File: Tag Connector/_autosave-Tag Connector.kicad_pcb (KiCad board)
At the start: 2 copper layers, 44.5 x 25.1 mm, 3 parts, among them J1 Conn_01x05_Male, J2 Conn_01x05_Male

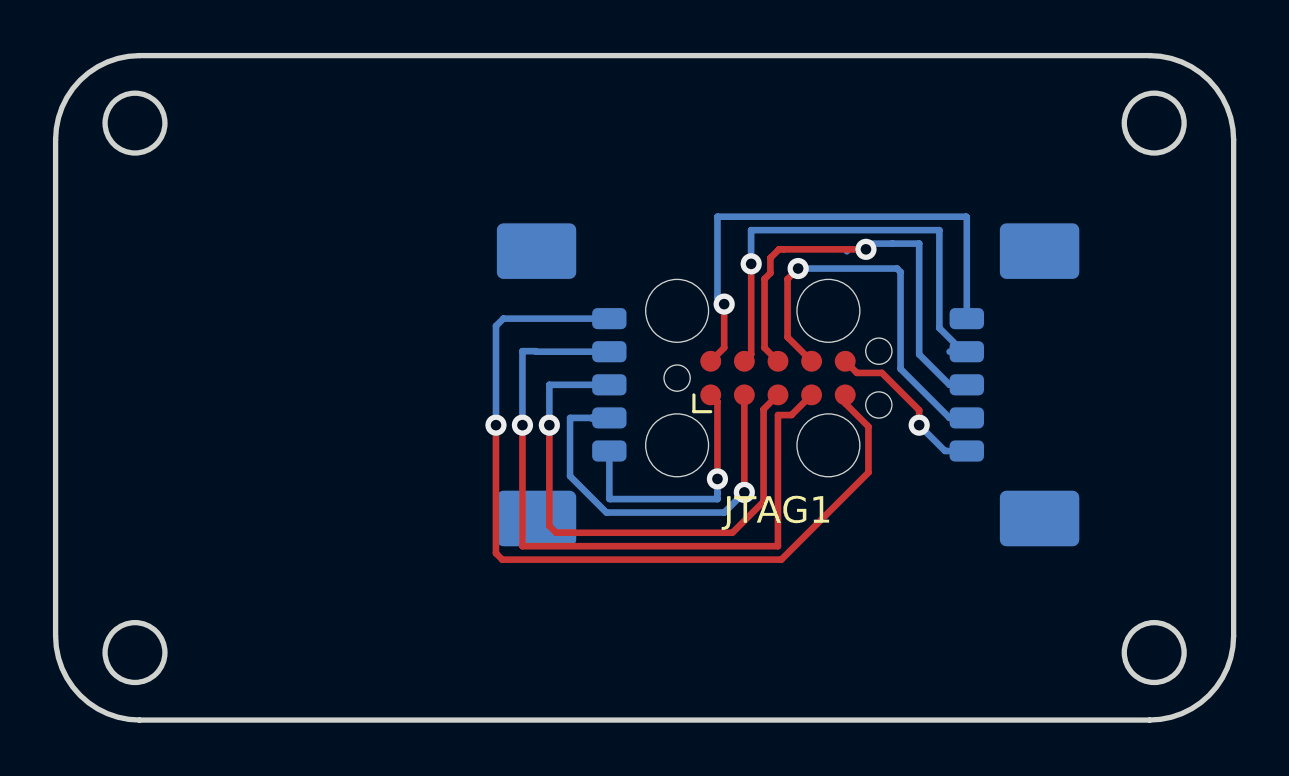
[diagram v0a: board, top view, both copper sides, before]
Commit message: updated manufacturing files
used correct dxf file to adjust the mounting holes on the PCB
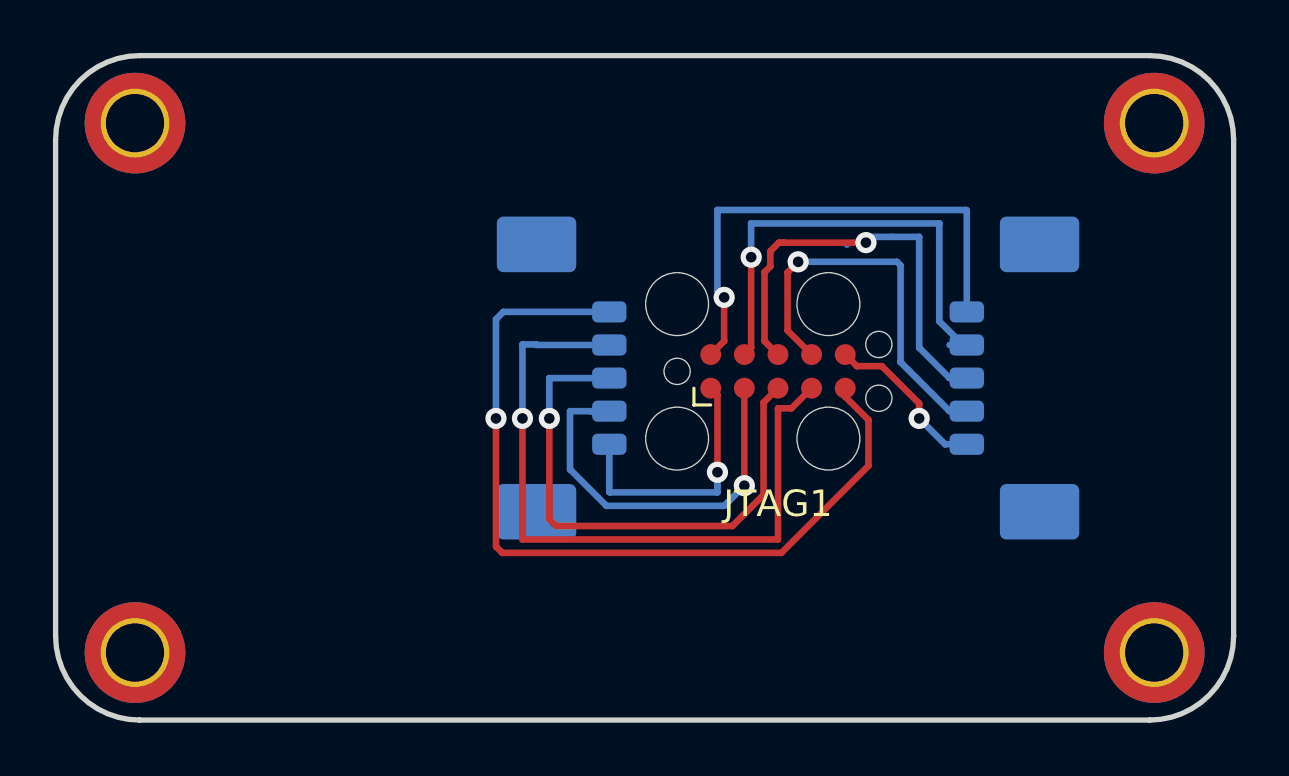
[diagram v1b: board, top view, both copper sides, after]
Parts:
- added ?: MountingHole_2.2mm_M2_DIN965_Pad_TopBottom, MountingHole:MountingHole_2.2mm_M2_DIN965_Pad_TopBottom, F.Cu at (136.9, 57.6)
- added REF**: MountingHole_2.2mm_M2_DIN965_Pad_TopBottom, MountingHole:MountingHole_2.2mm_M2_DIN965_Pad_TopBottom, F.Cu at (175.4, 77.6)
- added REF**: MountingHole_2.2mm_M2_DIN965_Pad_TopBottom, MountingHole:MountingHole_2.2mm_M2_DIN965_Pad_TopBottom, F.Cu at (175.4, 57.6)
- added REF**: MountingHole_2.2mm_M2_DIN965_Pad_TopBottom, MountingHole:MountingHole_2.2mm_M2_DIN965_Pad_TopBottom, F.Cu at (136.9, 77.6)
- moved JTAG1 0.25 mm to (161.2, 66.9)
- moved J1 0.25 mm to (153.6, 67.2)
- moved J2 0.25 mm to (169.6, 67.2)
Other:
- outline, holes or cut-outs redrawn
